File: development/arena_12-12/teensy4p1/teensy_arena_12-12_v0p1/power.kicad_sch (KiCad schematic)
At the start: 2 parts, among them J1 Barrel_Jack, SW1 SW_SPDT

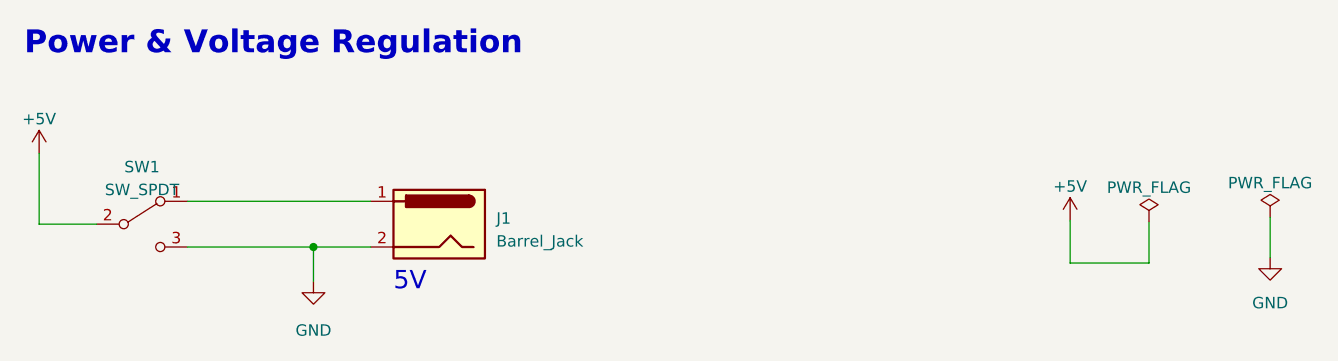
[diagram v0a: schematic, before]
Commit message: Worked on routing of ni 12-12 arena with vreg.
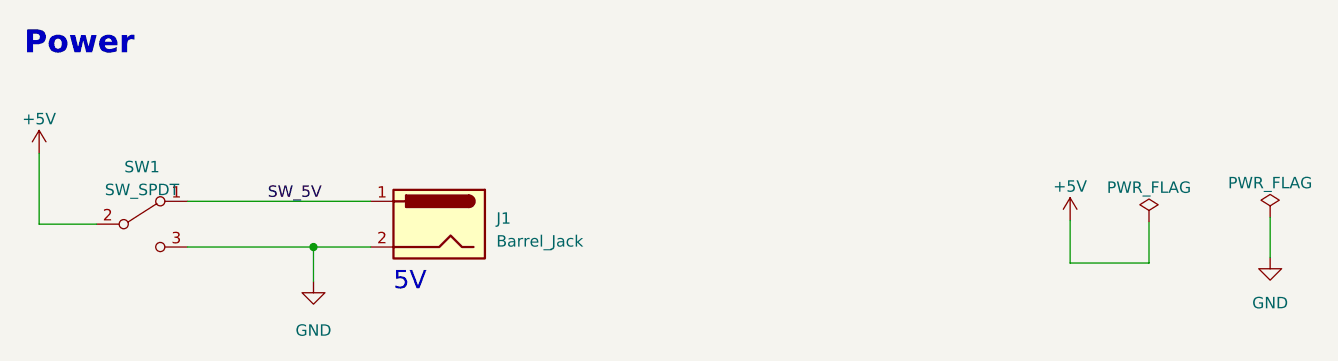
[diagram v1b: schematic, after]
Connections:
- net SW_5V: now reaches J1.1, SW1.1 (A)
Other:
- note added: "Power"
- note removed: "Power & Voltage Regulation"
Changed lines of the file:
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@@
     (effects (font (size 2.032 2.032)) (justify left bottom))
   )
-  (text "Power & Voltage Regulation" (at 115.189 21.082 0)
+  (text "Power" (at 115.189 21.082 0)
     (effects (font (size 2.54 2.54) (thickness 0.508) bold) (justify left bottom))
   )
+  (label "SW_5V" (at 142.24 37.084 0) (fields_autoplaced)
+    (effects (font (size 1.27 1.27)) (justify left bottom))
+  )
   (symbol (lib_id "power:+5V") (at 231.394 39.243 0) (unit 1)
